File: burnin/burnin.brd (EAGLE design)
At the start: 53 x 55 mm, 12 parts, among them M1 ARDUINO_R3_ICSP_NODIM, U1 TXB0104PWR

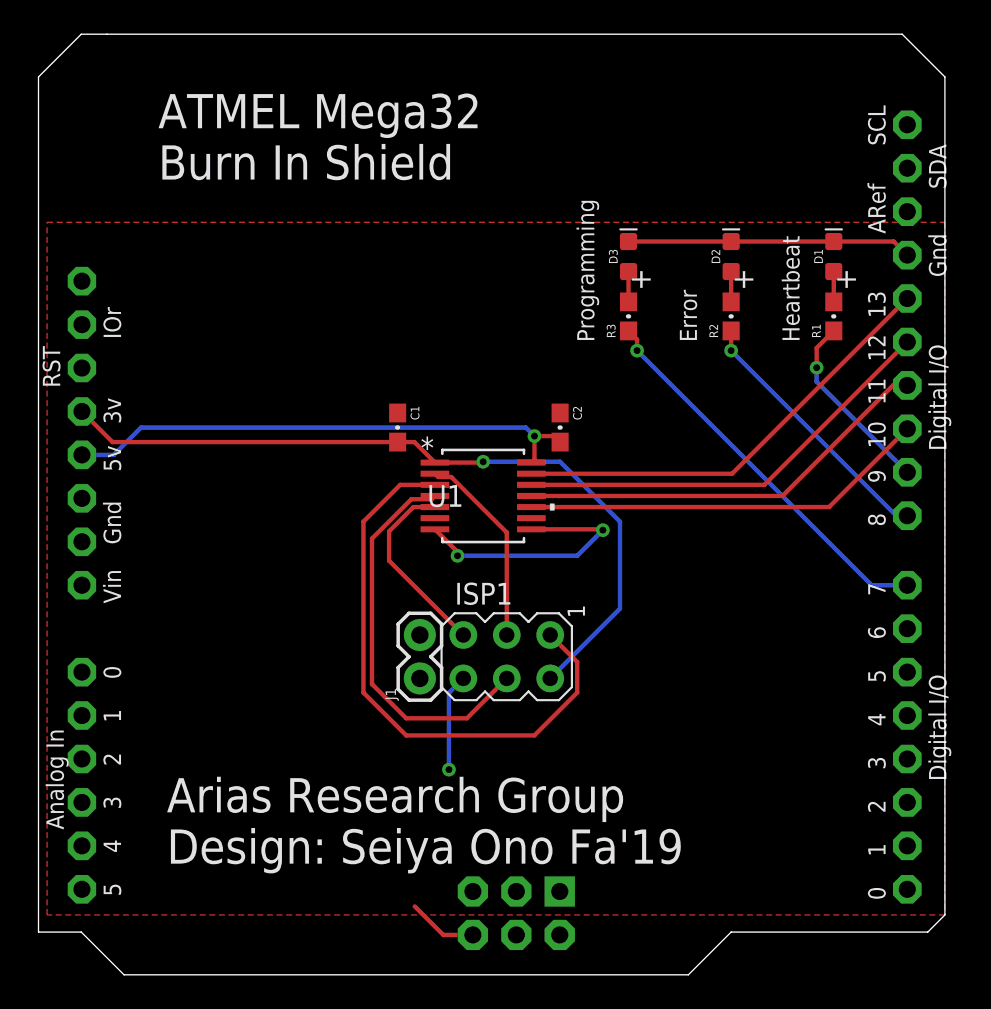
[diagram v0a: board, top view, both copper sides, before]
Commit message: fix burnin OE and make QFP MIPPE
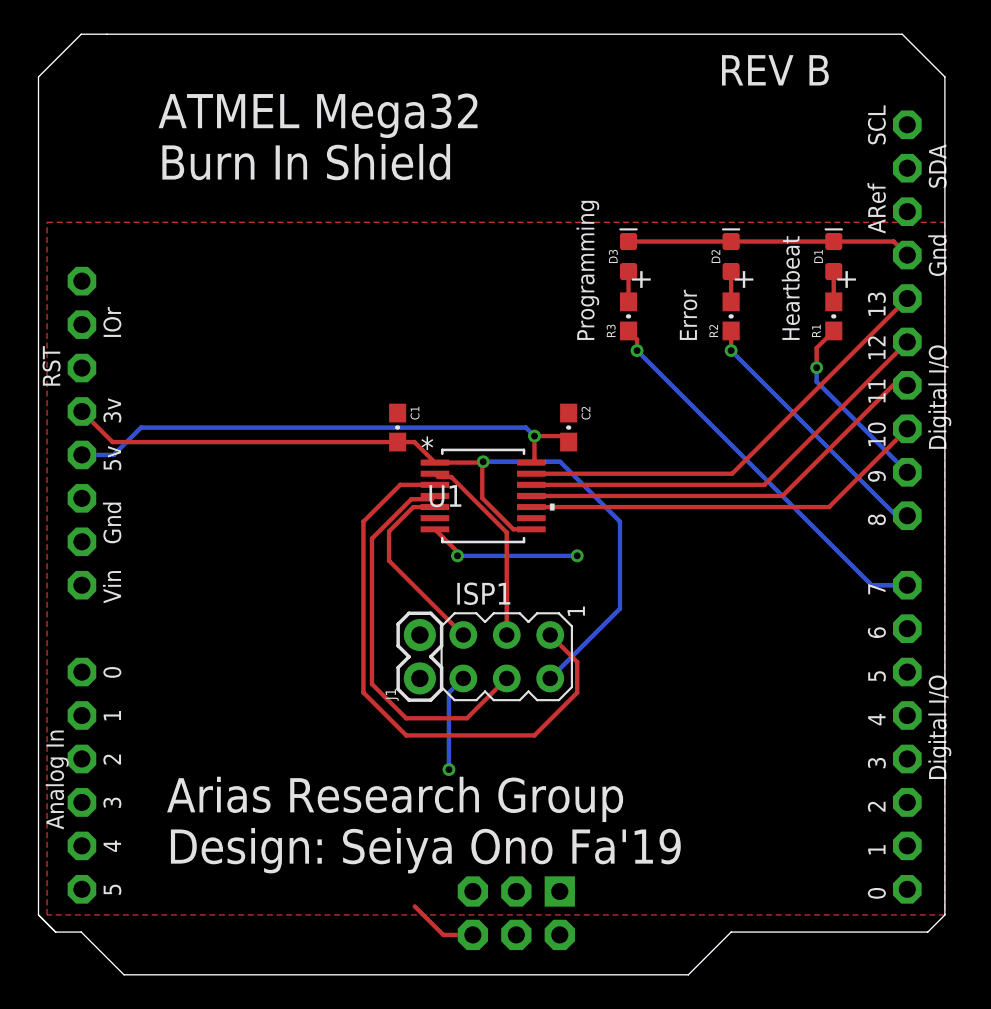
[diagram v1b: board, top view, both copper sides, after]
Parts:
- moved C2 0.50 mm to (31.0, 32.0)
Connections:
- net 3.3V: now also U1.8
- net GND: no longer U1.8
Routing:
- net GND: track 41.9 -> 35.5 mm
- net 3.3V: track 45.0 -> 50.7 mm
- net 5V: track 30.6 -> 31.1 mm
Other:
- outline, holes or cut-outs redrawn
- board text added: "REV B"

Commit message: finish 32u4 and rev c burnin
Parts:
- added ISP2: AVRISP-6, scono:AVRISP
- added J2: (no value), scono:1X02
- moved D3 4.00 mm to (38.5, 42.0)
- moved R3 4.00 mm to (38.5, 38.5)
- moved D2 2.00 mm to (42.5, 42.0)
- moved R2 2.00 mm to (42.5, 38.5)
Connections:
- net 5V: now also ISP2.2
- net GND: now also ISP2.6
- net MISO_5V: now also ISP2.1
- net MOSI_5V: now also ISP2.4
- net SCLK_5V: now also ISP2.3
- net SS_5V: now also ISP2.5
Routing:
- net SCLK_5V: track 26.2 -> 59.1 mm
- net MISO_5V: track 25.4 -> 57.5 mm, vias 0 -> 1
- net MOSI_5V: track 24.7 -> 54.3 mm
- net SS_5V: track 23.9 -> 51.3 mm
- net 5V: track 31.1 -> 43.9 mm
- net GND: track 35.5 -> 31.5 mm
- net PROGRAMMING: track 22.8 -> 20.0 mm
- net ERROR: track 15.4 -> 14.2 mm
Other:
- board text added: "ATMEL AVR Burn In Shield"
- board text added: "REV C"
- board text removed: "ATMEL Mega32 Burn In Shield"
- board text removed: "REV B"

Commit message: blaaahhhhh 328pb worked
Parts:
- removed C1, C2: 0.1uF, scono:0603-CAP
- removed ISP2: AVRISP-6, scono:AVRISP
- removed J2: (no value), scono:1X02
- removed U1: TXB0104PWR, scono:PW14
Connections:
- removed net MISO_3V: ISP1.1, U1.3
- removed net MOSI_3V: ISP1.4, U1.4
- removed net SCLK_3V: ISP1.3, U1.2
- removed net SS_3V: ISP1.5, U1.5
- net 3.3V: no longer C1.2, ISP1.2, U1.1, U1.8
- net 5V: now also ISP1.2; no longer C2.2, ISP2.2, U1.14
- net GND: no longer C1.1, C2.1, ISP2.6, U1.7
- net MISO_5V: now also ISP1.1; no longer ISP2.1, U1.12
- net MOSI_5V: now also ISP1.4; no longer ISP2.4, U1.11
- net SCLK_5V: now also ISP1.3; no longer ISP2.3, U1.13
- net SS_5V: now also ISP1.5; no longer ISP2.5, U1.10
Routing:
- net 3.3V: track 50.7 -> 0.00 mm, vias 1 -> 0
- net MISO_3V: track 33.7 -> 0.00 mm
- net MISO_5V: track 57.5 -> 28.0 mm, vias 1 -> 0
- net SCLK_5V: track 59.1 -> 31.6 mm
- net MOSI_3V: track 22.9 -> 0.00 mm
- net SS_5V: track 51.3 -> 31.0 mm, vias 0 -> 1
- net MOSI_5V: track 54.3 -> 35.1 mm, vias 0 -> 1
- net GND: track 31.5 -> 16.7 mm, vias 3 -> 0
- net SCLK_3V: track 11.6 -> 0.00 mm
- net SS_3V: track 11.1 -> 0.00 mm
- net 5V: track 43.9 -> 36.6 mm, vias 1 -> 0
